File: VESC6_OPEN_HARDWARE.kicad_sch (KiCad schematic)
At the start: 20 parts, among them P1 USB_OTG, P2 TS_CAN, P3 SWD, P4 HALL/Encoder, P5 TS_CAN, P7 Custom

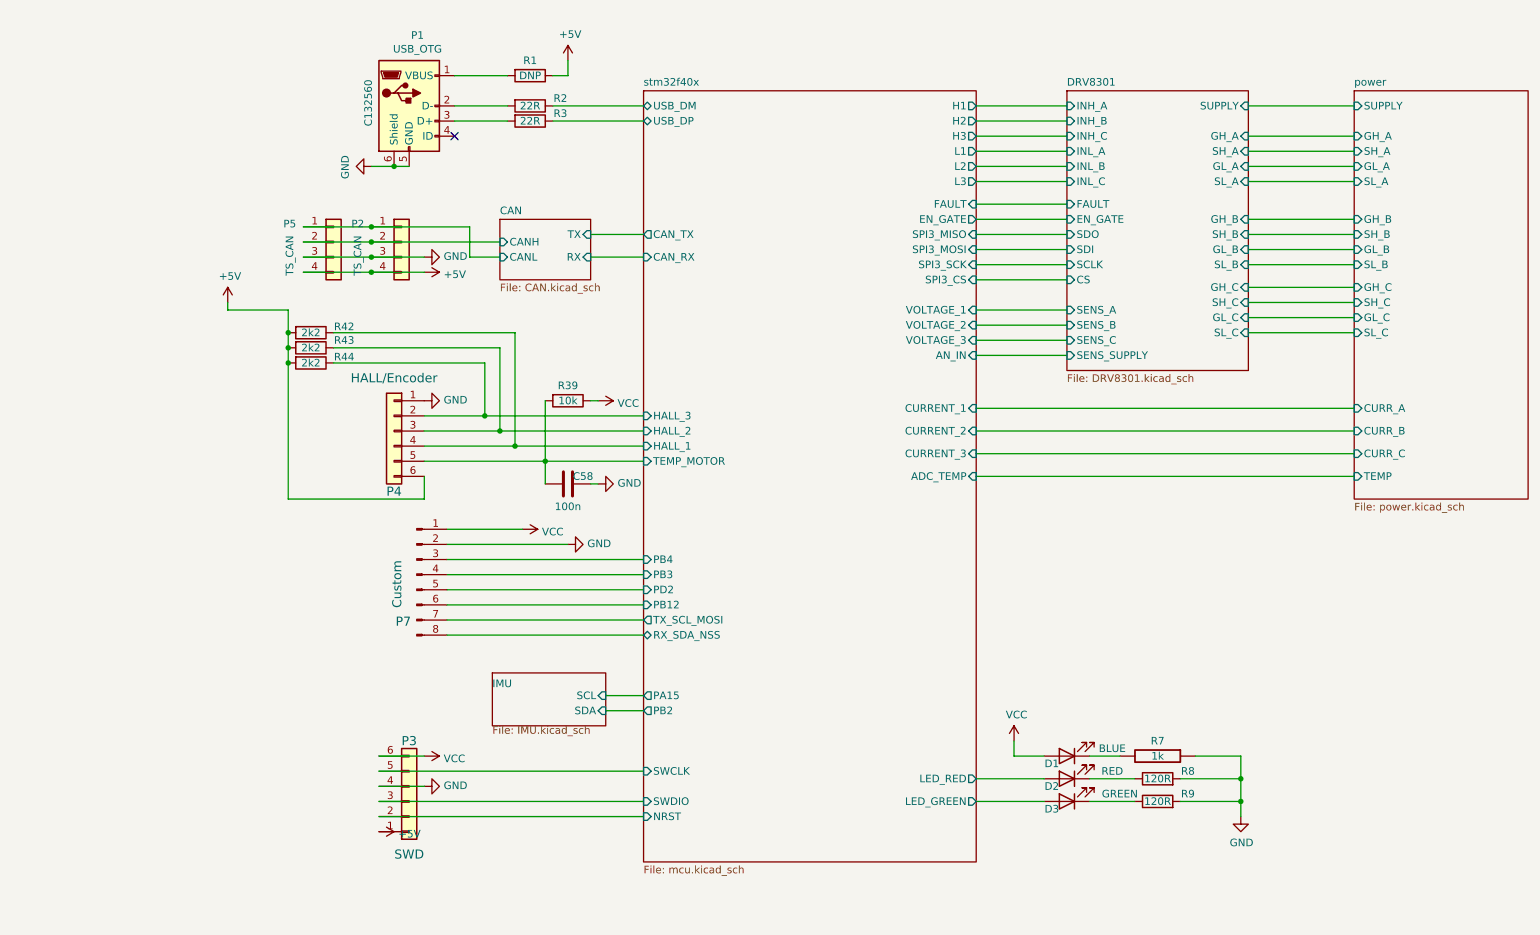
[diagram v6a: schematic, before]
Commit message: changed connectors, needs final routing and drc
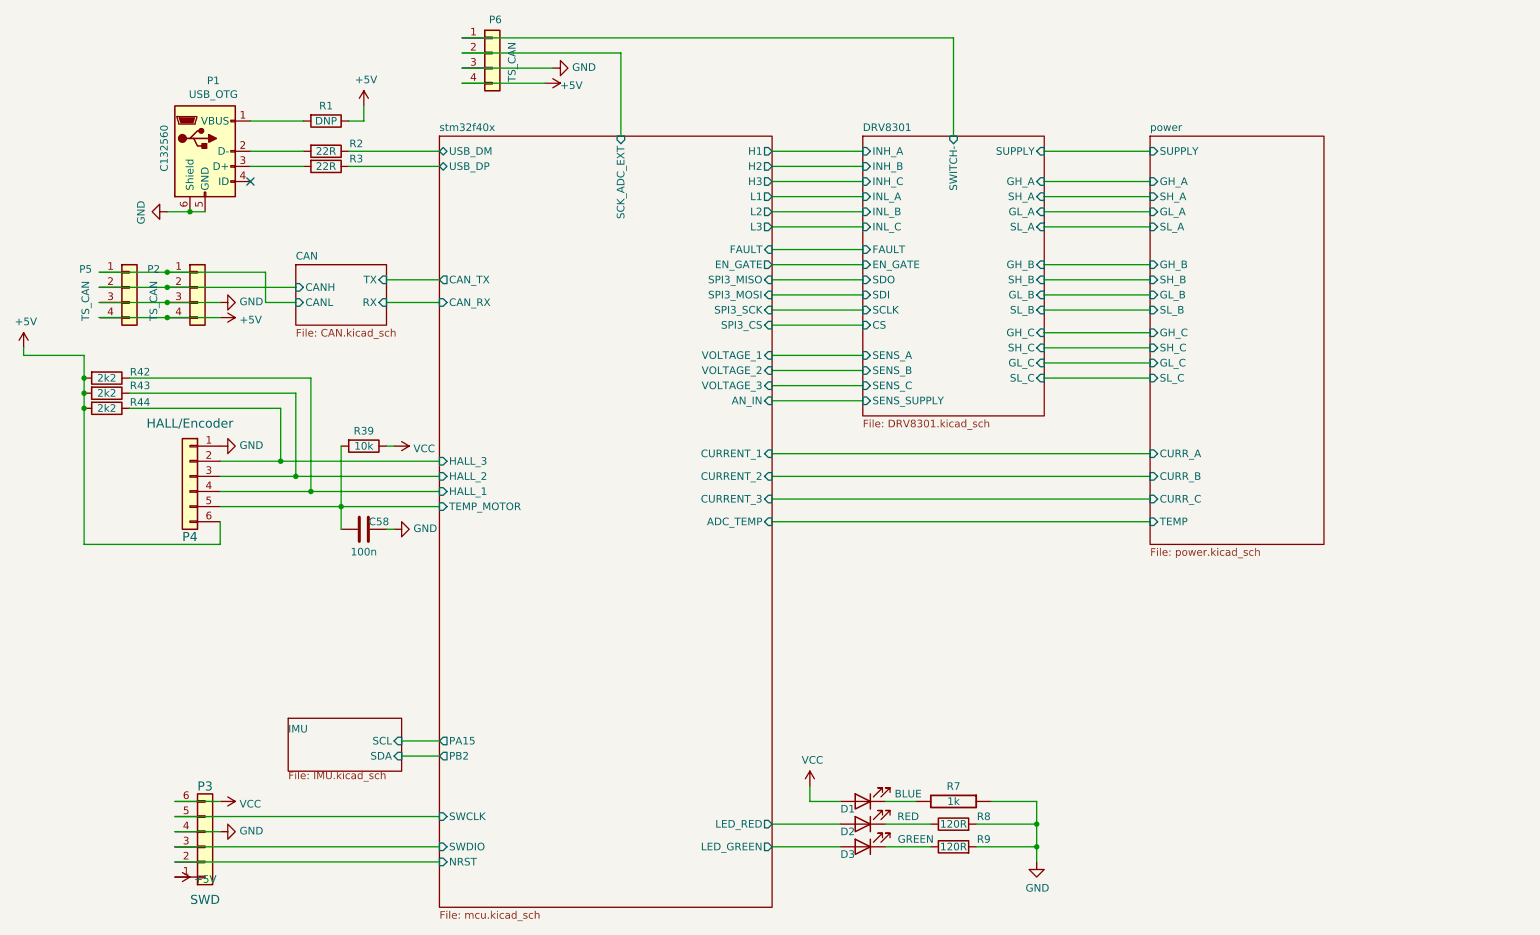
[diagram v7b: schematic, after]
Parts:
- removed P7: Custom, Connector_PinSocket_1.27mm:PinSocket_1x08_P1.27mm_Vertical, symbol Connector:Conn_01x08_Pin
- added P6: TS_CAN, Connector_JST:JST_SH_SM04B-SRSS-TB_1x04-1MP_P1.00mm_Horizontal, symbol Connector_Generic:Conn_01x04
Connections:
- net +5V: now also P6.4 (Pin_4)
- net GND: now also P6.3 (Pin_3)
- new net DRV8301/SWITCH-: P6.1 (Pin_1)
- new net stm32f40x/SCK_ADC_EXT: P6.2 (Pin_2)
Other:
- sheet DRV8301 ports: added SWITCH-; removed none
- sheet stm32f40x ports: added SCK_ADC_EXT; removed PB12, PB3, PB4, PD2, RX_SDA_NSS, TX_SCL_MOSI
- moved on the sheet: C58, D1, D2, D3, P1, P2, P3, P4, P5, R1, R2, R3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

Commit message: Finished routing
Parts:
- D1: LCSC part no. C72041 -> C2288
- D3: LCSC part no. C72043 -> C12624
- P2: value TS_CAN -> CAN2; LCSC part no. C160404 -> C23390337
- P3: LCSC part no. C160405 -> 23390339
- P5: value TS_CAN -> CAN1; LCSC part no. C160404 -> C23390337
- P6: value TS_CAN -> ADC_SWITCH; LCSC part no. C160404 -> C23390337
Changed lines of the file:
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@@
 			)
 		)
-		(property "Value" "TS_CAN"
+		(property "Value" "CAN2"
 			(at 45.974 61.976 90)
 			(effects
@@
 			)
 		)
-		(property "LCSC part no." "C160404"
+		(property "LCSC part no." "C23390337"
 			(at 53.34 59.69 0)
 			(effects
@@
 			)
 		)
-		(property "LCSC part no." "C72041"
+		(property "LCSC part no." "C2288"
 			(at 165.1 146.05 0)
 			(effects
@@
 			)
 		)
-		(property "LCSC part no." "C72043"
+		(property "LCSC part no." "C12624"
 			(at 165.1 153.67 0)
 			(effects
@@
 			)
 		)
-		(property "Value" "TS_CAN"
+		(property "Value" "CAN1"
 			(at 34.544 61.976 90)
 			(effects
@@
 			)
 		)
-		(property "LCSC part no." "C160404"
+		(property "LCSC part no." "C23390337"
 			(at 41.91 59.69 0)
 			(effects
@@
 			)
 		)
-		(property "Value" "TS_CAN"
+		(property "Value" "ADC_SWITCH"
 			(at 106.172 21.844 90)
 			(effects
@@
 			)
 		)
-		(property "LCSC part no." "C160404"
+		(property "LCSC part no." "C23390337"
 			(at 102.87 20.32 0)
 			(effects
@@
 			)
 		)
-		(property "LCSC part no." "C160405"
+		(property "LCSC part no." "23390339"
 			(at 54.61 153.67 0)
 			(effects
